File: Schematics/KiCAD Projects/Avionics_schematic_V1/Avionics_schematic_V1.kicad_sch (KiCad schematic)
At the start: 6 parts, among them J1 SD_Card_Breakout, SW1 SW_Push, U1 Pico

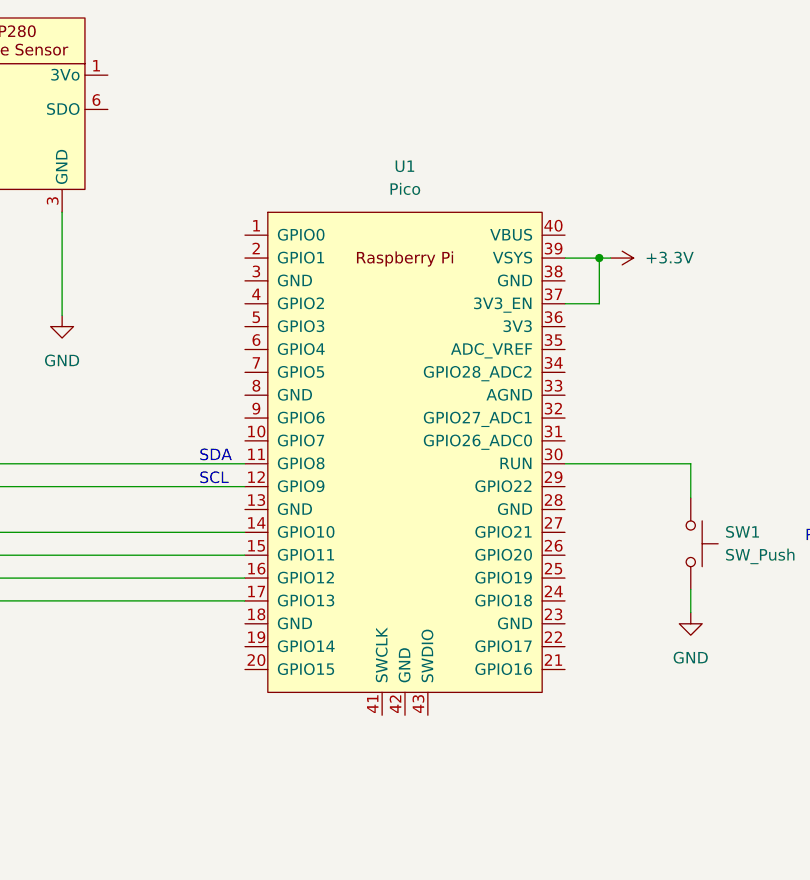
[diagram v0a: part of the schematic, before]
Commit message: Updated library paths for proper migration
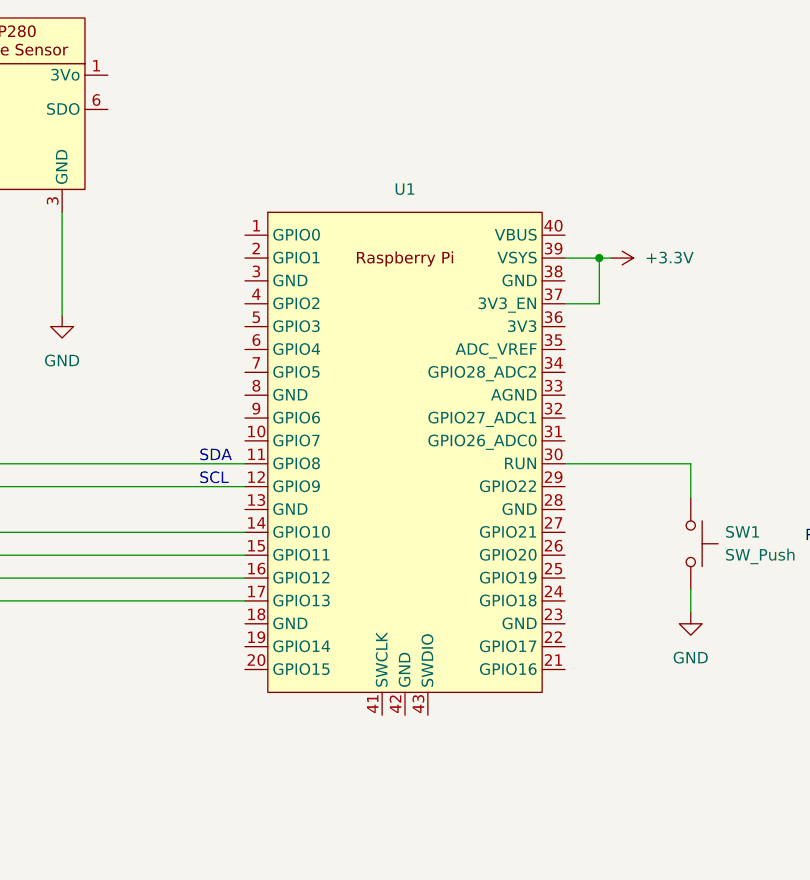
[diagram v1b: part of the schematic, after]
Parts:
- removed U1: Pico, RPi_Pico:RPi_Pico_SMD_TH, symbol RPi_Pico:Pico
- added U1: ~, symbol Breakout_boards:Raspberry_Pi_Pico
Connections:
- net +3.3V: now also U1.37 (3V3_EN), U1.39 (VSYS)
- net at SW1.1: now also U1.30 (RUN)
- net at U2.3 (SCL), U3.4 (SCK): now also U1.12 (GPIO9)
- net at U2.4 (SDA), U3.5 (SDI): now also U1.11 (GPIO8)
- net at J1.4 (CLK): now also U1.14 (GPIO10)
- net at J1.5 (DO): now also U1.16 (GPIO12)
- net at J1.6 (DI): now also U1.15 (GPIO11)
- net at J1.7 (CS): now also U1.17 (GPIO13)
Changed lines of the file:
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@@
+    )
+  )
+  (symbol (lib_id "Breakout_boards:Raspberry_Pi_Pico") (at 168.91 124.46 0) (unit 1)
+    (in_bom yes) (on_board yes) (dnp no) (fields_autoplaced)
+    (property "Reference" "U1" (at 184.15 68.58 0)
+      (effects (font (size 1.27 1.27)))
+    )
+    (property "Value" "~" (at 168.91 124.46 0)
+      (effects (font (size 1.27 1.27)))
+    )
+    (property "Footprint" "" (at 168.91 124.46 0)
+      (effects (font (size 1.27 1.27)) hide)
+    )
+    (property "Datasheet" "" (at 168.91 124.46 0)
+      (effects (font (size 1.27 1.27)) hide)
+    )
+    (pin "37")
+    (pin "40")
+    (pin "5")
+    (pin "31")
+    (pin "14")
+    (pin "41")
+    (pin "1")
+    (pin "25")
+    (pin "9")
+    (pin "2")
+    (pin "43")
+    (pin "21")
+    (pin "30")
+    (pin "33")
+    (pin "23")
+    (pin "7")
+    (pin "22")
+    (pin "29")
+    (pin "35")
+    (pin "28")
+    (pin "38")
+    (pin "3")
+    (pin "4")
+    (pin "19")
+    (pin "39")
+    (pin "42")
+    (pin "32")
+    (pin "6")
+    (pin "11")
+    (pin "17")
+    (pin "34")
+    (pin "10")
+    (pin "13")
+    (pin "24")
+    (pin "8")
+    (pin "15")
+    (pin "20")
+    (pin "36")
+    (pin "27")
+    (pin "12")
+    (pin "16")
+    (pin "18")
+    (pin "26")
+    (instances
+      (project "Avionics_schematic_V1"
+        (path "/73c2587e-5580-40a9-b11a-10d35d57510a"
+          (reference "U1") (unit 1)
+        )
+      )
     )
   )
@@
         )
       )
-    )
-  )
-  (symbol (lib_id "RPi_Pico:Pico") (at 184.15 97.79 0) (unit 1)
-    (in_bom yes) (on_board yes) (dnp no) (fields_autoplaced)
-    (property "Reference" "U1" (at 184.15 66.04 0)
-      (effects (font (size 1.27 1.27)))
-    )
-    (property "Value" "Pico" (at 184.15 68.58 0)
-      (effects (font (size 1.27 1.27)))
-    )
-    (property "Footprint" "RPi_Pico:RPi_Pico_SMD_TH" (at 184.15 97.79 90)
-      (effects (font (size 1.27 1.27)) hide)
-    )
-    (property "Datasheet" "" (at 184.15 97.79 0)
-      (effects (font (size 1.27 1.27)) hide)
-    )
-    (pin "16")
-    (pin "42")
-    (pin "14")
-    (pin "19")
-    (pin "28")
-    (pin "29")
-    (pin "3")
-    (pin "35")
-    (pin "36")
-    (pin "11")
-    (pin "25")
-    (pin "13")
-    (pin "27")
-    (pin "21")
-    (pin "22")
-    (pin "43")
-    (pin "5")
-    (pin "39")
-    (pin "6")
-    (pin "7")
-    (pin "8")
-    (pin "1")
-    (pin "15")
-    (pin "12")
-    (pin "23")
-    (pin "30")
-    (pin "33")
-    (pin "24")
-    (pin "38")
-    (pin "9")
-    (pin "17")
-    (pin "10")
-    (pin "4")
-    (pin "2")
-    (pin "20")
-    (pin "40")
-    (pin "37")
-    (pin "18")
-    (pin "26")
-    (pin "31")
-    (pin "32")
-    (pin "34")
-    (pin "41")
-    (instances
-      (project "Avionics_schematic_V1"
-        (path "/73c2587e-5580-40a9-b11a-10d35d57510a"
-          (reference "U1") (unit 1)
-        )
-      )

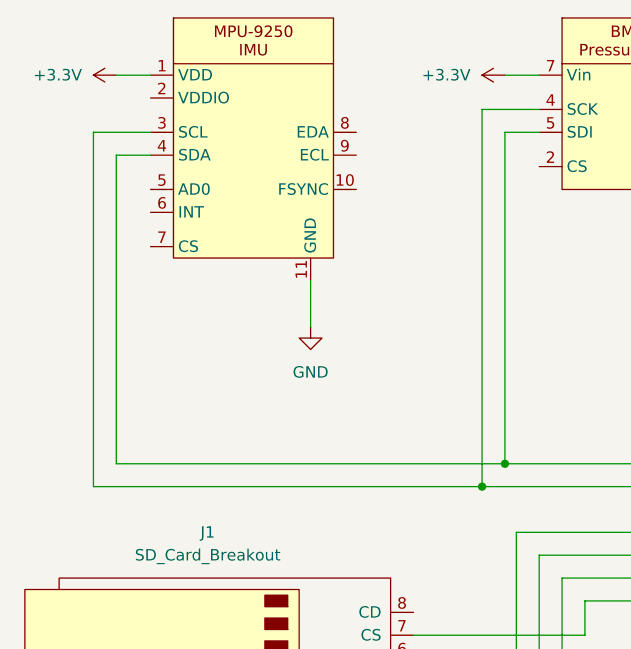
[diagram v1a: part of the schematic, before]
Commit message: Added BNO055 to library and replaced MPU-9250
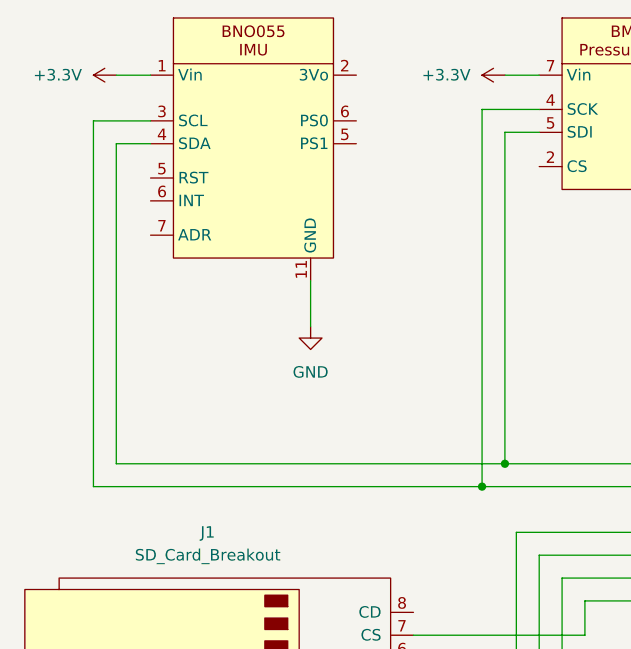
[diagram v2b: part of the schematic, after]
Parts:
- removed U2: ~, symbol Breakout_boards:MPU-9250_breakout
- added U4: ~, symbol Breakout_boards:BNO055
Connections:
- net +3.3V: now also U4.1 (Vin)
- net GND: now also U4.11 (GND)
- net at U1.12 (GPIO9), U3.4 (SCK): now also U4.3 (SCL)
- net at U1.11 (GPIO8), U3.5 (SDI): now also U4.4 (SDA)
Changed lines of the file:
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@@
     (stroke (width 0) (type default))
   )
-  (wire (pts (xy 81.28 64.77) (xy 81.28 99.06))
+  (wire (pts (xy 81.28 63.5) (xy 81.28 99.06))
     (stroke (width 0) (type default))
   )
@@
     (stroke (width 0) (type default))
   )
-  (wire (pts (xy 78.74 62.23) (xy 78.74 101.6))
+  (wire (pts (xy 78.74 60.96) (xy 78.74 101.6))
     (stroke (width 0) (type default))
   )
@@
     (stroke (width 0) (type default))
   )
-  (wire (pts (xy 85.09 62.23) (xy 78.74 62.23))
+  (wire (pts (xy 85.09 60.96) (xy 78.74 60.96))
     (stroke (width 0) (type default))
   )
@@
     (stroke (width 0) (type default))
   )
-  (wire (pts (xy 85.09 64.77) (xy 81.28 64.77))
+  (wire (pts (xy 85.09 63.5) (xy 81.28 63.5))
     (stroke (width 0) (type default))
   )
@@
         (path "/73c2587e-5580-40a9-b11a-10d35d57510a"
           (reference "SW1") (unit 1)
-        )
-      )
-    )
-  )
-  (symbol (lib_id "Breakout_boards:MPU-9250_breakout") (at 96.52 62.23 0) (unit 1)
-    (in_bom yes) (on_board yes) (dnp no) (fields_autoplaced)
-    (property "Reference" "U2" (at 96.52 52.07 0)
-      (effects (font (size 1.27 1.27)) hide)
-    )
-    (property "Value" "~" (at 93.98 60.96 0)
-      (effects (font (size 1.27 1.27)))
-    )
-    (property "Footprint" "" (at 93.98 60.96 0)
-      (effects (font (size 1.27 1.27)) hide)
-    )
-    (property "Datasheet" "" (at 93.98 60.96 0)
-      (effects (font (size 1.27 1.27)) hide)
-    )
-    (pin "2")
-    (pin "9")
-    (pin "1")
-    (pin "6")
-    (pin "7")
-    (pin "8")
-    (pin "4")
-    (pin "3")
-    (pin "11")
-    (pin "5")
-    (pin "10")
-    (instances
-      (project "Avionics_schematic_V1"
-        (path "/73c2587e-5580-40a9-b11a-10d35d57510a"
-          (reference "U2") (unit 1)
         )
       )
@@
         )
       )
+    )
+  )
+  (symbol (lib_id "Breakout_boards:BNO055") (at 87.63 76.2 0) (unit 1)
+    (in_bom yes) (on_board yes) (dnp no) (fields_autoplaced)
+    (property "Reference" "U4" (at 87.63 74.93 0)
+      (effects (font (size 1.27 1.27)) hide)
+    )
+    (property "Value" "~" (at 87.63 74.93 0)
+      (effects (font (size 1.27 1.27)))
+    )
+    (property "Footprint" "" (at 87.63 74.93 0)
+      (effects (font (size 1.27 1.27)) hide)
+    )
+    (property "Datasheet" "https://cdn-learn.adafruit.com/downloads/pdf/adafruit-bno055-absolute-orientation-sensor.pdf" (at 87.63 74.93 0)
+      (effects (font (size 1.27 1.27)) hide)
+    )
+    (pin "5")
+    (pin "7")
+    (pin "5")
+    (pin "1")
+    (pin "3")
+    (pin "4")
+    (pin "6")
+    (pin "6")
+    (pin "11")
+    (pin "2")
+    (instances
+      (project "Avionics_schematic_V1"
+        (path "/73c2587e-5580-40a9-b11a-10d35d57510a"
+          (reference "U4") (unit 1)
+        )
+      )

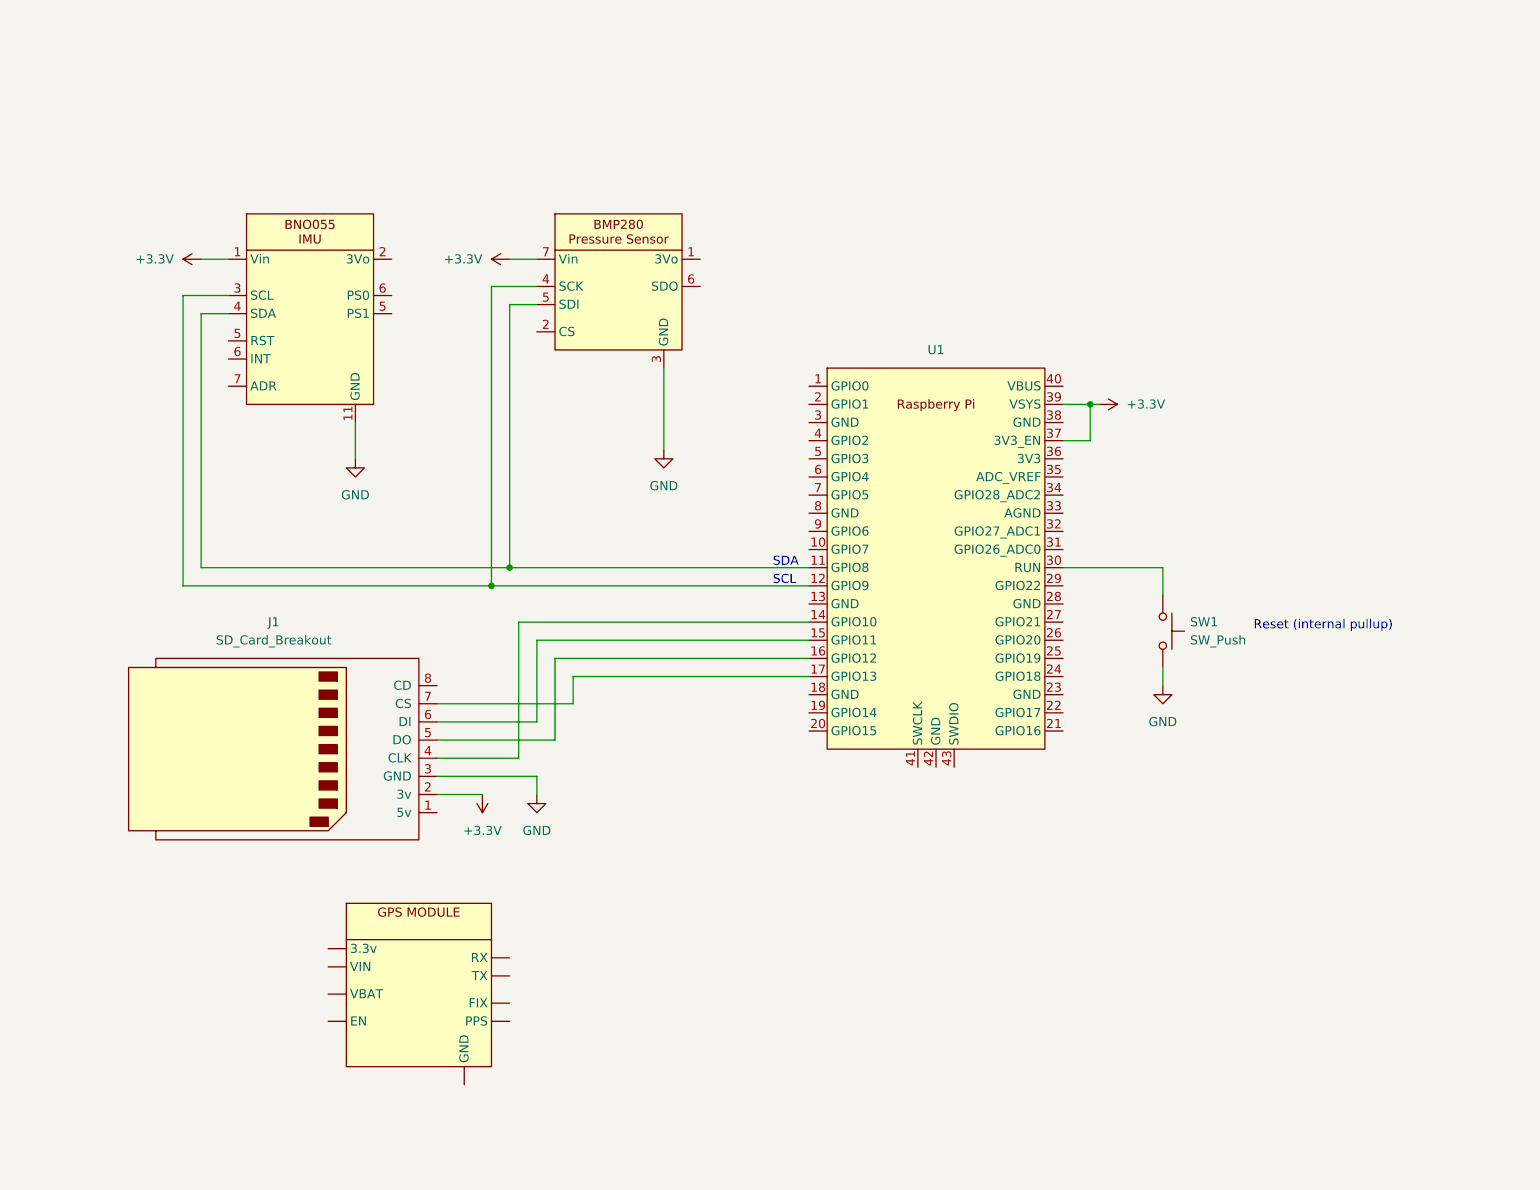
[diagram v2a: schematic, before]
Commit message: Added flash storage
added flash breakout to library and schematic
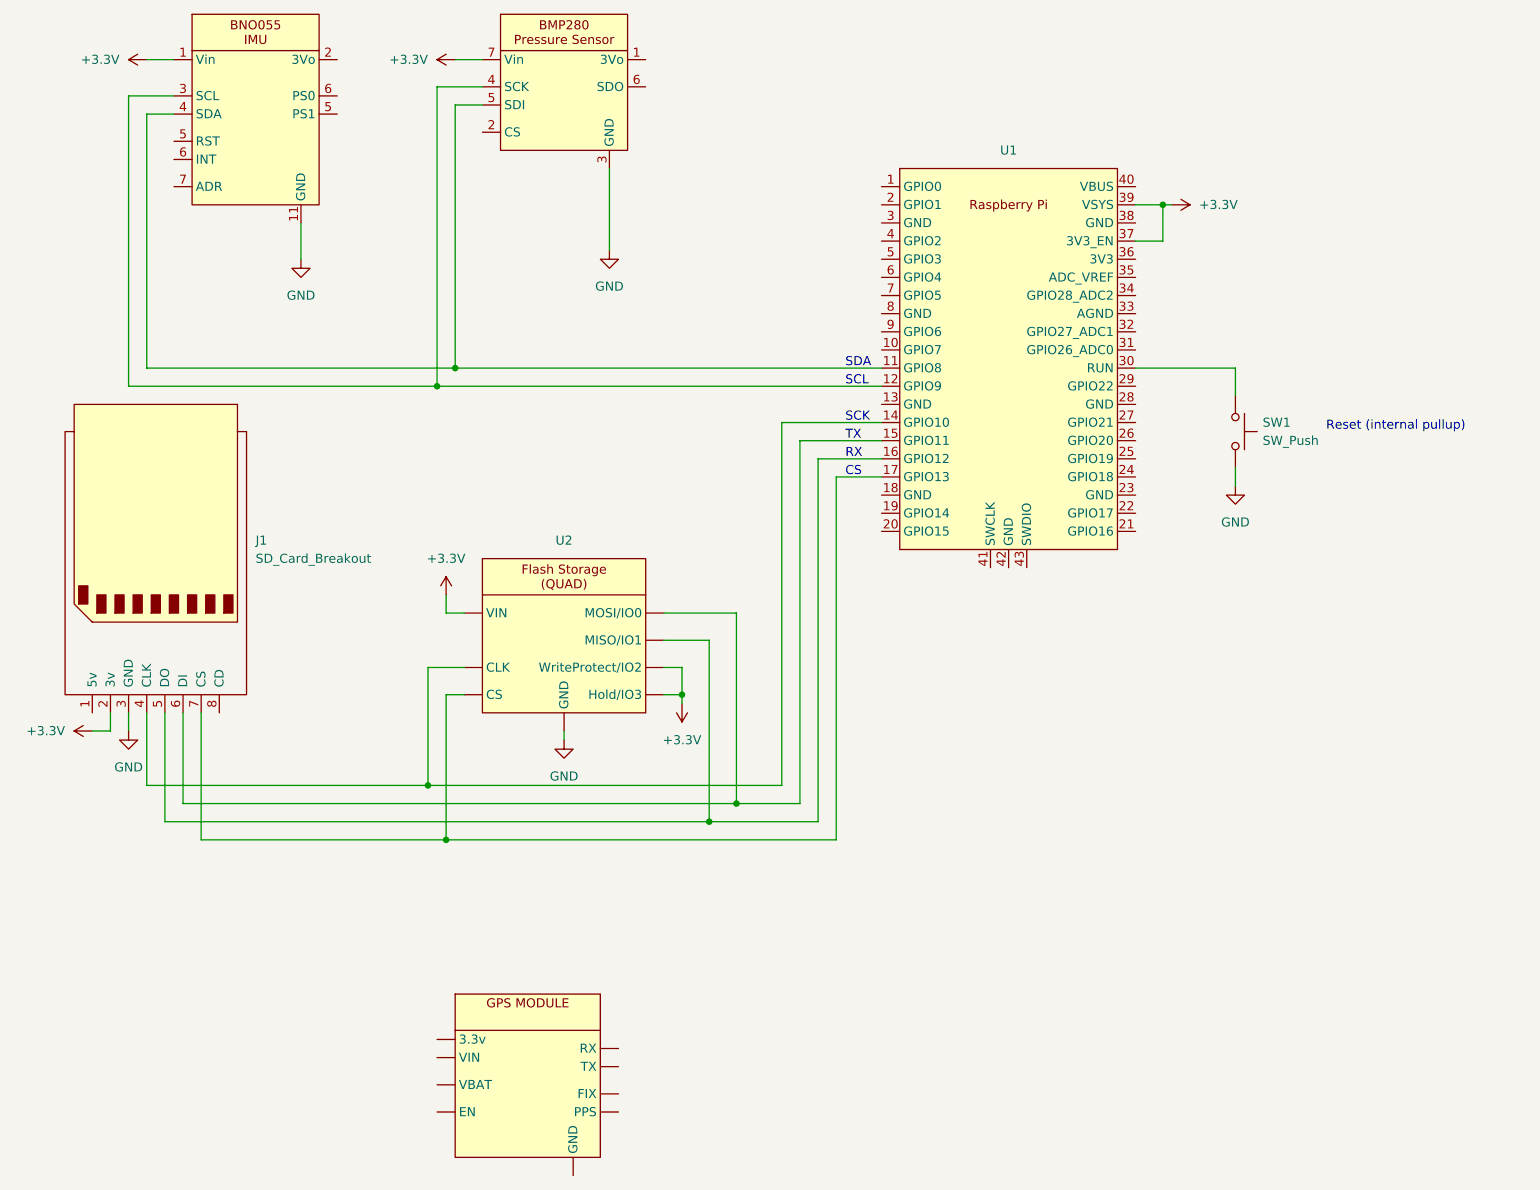
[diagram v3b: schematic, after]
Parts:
- added U2: ~, symbol Breakout_boards:Flash_Breakout
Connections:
- net +3.3V: now also U2. (WriteProtect/IO2)
- net GND: now also U2. (WriteProtect/IO2)
- net at J1.4 (CLK), U1.14 (GPIO10): now also U2. (WriteProtect/IO2)
- net at J1.5 (DO), U1.16 (GPIO12): now also U2. (WriteProtect/IO2)
- net at J1.6 (DI), U1.15 (GPIO11): now also U2. (WriteProtect/IO2)
- net at J1.7 (CS), U1.17 (GPIO13): now also U2. (WriteProtect/IO2)
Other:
- note added: "CS"
- note added: "RX"
- note added: "SCK"
- note added: "TX"
- moved on the sheet: J1, SW1, U1
